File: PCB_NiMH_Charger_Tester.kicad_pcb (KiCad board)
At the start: 2 copper layers, 94.9 x 77.5 mm, 63 parts, among them J1 USB_C_Receptacle_PowerOnly_6P, J2 USB_C_Receptacle_USB2.0_16P, J3 UPDI v2 header, J4 SSD1306, J5 Serial Header, Q1 DTC114EL, Q2 DTA114EL, Q3 MTB060P06I3, Q4 MTA100N10KRI3, SW1 SW_Push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

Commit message: Revert resistor values
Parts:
- R10, R11: value 4.7k -> 1k
- R12, R15: value 47k -> 10k
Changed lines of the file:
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@@
 	(title_block
 		(title "NiMH Charger & Tester")
-		(date "2025-09-26")
+		(date "2025-10-15")
 		(rev "2")
 		(company "K.Takata")
@@
 			)
 		)
-		(property "Value" "4.7k"
+		(property "Value" "1k"
 			(at 1.27 2.37 0)
 			(layer "F.Fab")
@@
 			)
 		)
-		(property "Value" "47k"
+		(property "Value" "10k"
 			(at 1.27 2.37 0)
 			(layer "F.Fab")
@@
 			)
 		)
-		(property "Value" "47k"
+		(property "Value" "10k"
 			(at 1.27 2.37 0)
 			(layer "F.Fab")
@@
 			)
 		)
-		(property "Value" "4.7k"
+		(property "Value" "1k"
 			(at 1.27 2.37 0)
 			(layer "F.Fab")

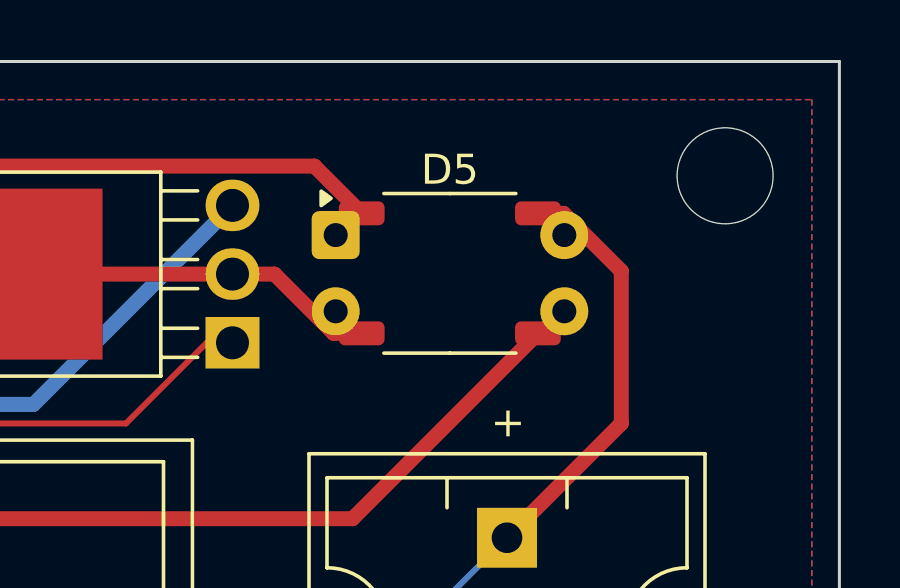
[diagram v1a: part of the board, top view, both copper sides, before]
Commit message: Fix D6 footprint
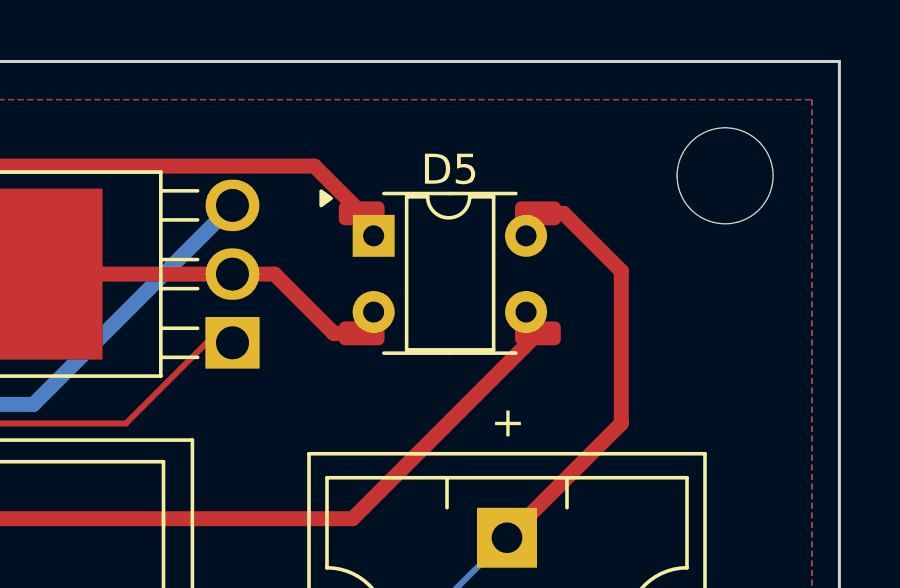
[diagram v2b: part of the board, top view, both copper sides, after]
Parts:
- D6: footprint Package_DIP:DIP-4_W7.62mm -> Diode_THT:Diode_Bridge_DIP-4_W5.08mm_P2.54mm
- moved D6 1.27 mm to (128.9, 29.9)
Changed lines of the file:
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@@
 		)
 	)
-	(footprint "Package_DIP:DIP-4_W7.62mm"
+	(footprint "Diode_THT:Diode_Bridge_DIP-4_W5.08mm_P2.54mm"
 		(layer "F.Cu")
-		(at 127.64 29.9162)
-		(descr "4-lead though-hole mounted DIP package, row spacing 7.62mm (300 mils)")
-		(tags "THT DIP DIL PDIP 2.54mm 7.62mm 300mil")
+		(at 128.905 29.9412)
+		(descr "4-lead dip package for diode bridges, row spacing 5.08mm, pin-spacing 2.54mm, see http://www.vishay.com/docs/88898/b2m.pdf")
+		(tags "DIL DIP PDIP 5.08mm 2.54")
 		(property "Reference" "D6"
-			(at 3.81 -2.33 0)
+			(at 2.5 -2.2 0)
 			(layer "F.SilkS")
 			(hide yes)
@@
 		)
 		(property "Value" "S1ZB20"
-			(at 3.81 4.87 0)
+			(at 2.3 4.6 0)
 			(layer "F.Fab")
 			(effects
@@
 		(property "Datasheet" "https://www.mouser.jp/datasheet/2/366/J534S1ZB-1203344.pdf"
 			(at 0 0 0)
+			(unlocked yes)
 			(layer "F.Fab")
 			(hide yes)
@@
 		(property "Description" "Diode Bridge, 200V Vrms, 1A If, DIP-4"
 			(at 0 0 0)
+			(unlocked yes)
 			(layer "F.Fab")
 			(hide yes)
@@
 		(sheetfile "PCB_NiMH_Charger_Tester.kicad_sch")
 		(attr through_hole dnp)
-		(fp_rect
-			(start -1.06 -1.52)
-			(end 8.67 4.07)
-			(stroke
-				(width 0.05)
-				(type solid)
-			)
-			(fill no)
-			(layer "F.CrtYd")
-		)
-		(fp_line
-			(start 0.635 -0.27)
-			(end 1.635 -1.27)
-			(stroke
-				(width 0.1)
-				(type solid)
-			)
-			(layer "F.Fab")
-		)
-		(fp_line
-			(start 0.635 3.81)
-			(end 0.635 -0.27)
-			(stroke
-				(width 0.1)
-				(type solid)
-			)
-			(layer "F.Fab")
-		)
-		(fp_line
-			(start 1.635 -1.27)
-			(end 6.985 -1.27)
-			(stroke
-				(width 0.1)
-				(type solid)
-			)
-			(layer "F.Fab")
-		)
-		(fp_line
-			(start 6.985 -1.27)
-			(end 6.985 3.81)
-			(stroke
-				(width 0.1)
-				(type solid)
-			)
-			(layer "F.Fab")
-		)
-		(fp_line
-			(start 6.985 3.81)
-			(end 0.635 3.81)
-			(stroke
-				(width 0.1)
+		(fp_line
+			(start 1.1 -1.3)
+			(end 1.1 3.8)
+			(stroke
+				(width 0.12)
+				(type solid)
+			)
+			(layer "F.SilkS")
+		)
+		(fp_line
+			(start 1.1 3.8)
+			(end 4 3.8)
+			(stroke
+				(width 0.12)
+				(type solid)
+			)
+			(layer "F.SilkS")
+		)
+		(fp_line
+			(start 1.8 -1.3)
+			(end 1.1 -1.3)
+			(stroke
+				(width 0.12)
+				(type solid)
+			)
+			(layer "F.SilkS")
+		)
+		(fp_line
+			(start 4 -1.3)
+			(end 3.2 -1.3)
+			(stroke
+				(width 0.12)
+				(type solid)
+			)
+			(layer "F.SilkS")
+		)
+		(fp_line
+			(start 4 3.8)
+			(end 4 -1.3)
+			(stroke
+				(width 0.12)
+				(type solid)
+			)
+			(layer "F.SilkS")
+		)
+		(fp_arc
+			(start 3.2 -1.3)
+			(mid 2.5 -0.6)
+			(end 1.8 -1.3)
+			(stroke
+				(width 0.12)
+				(type solid)
+			)
+			(layer "F.SilkS")
+		)
+		(fp_line
+			(start -0.95 -1.35)
+			(end -0.95 3.85)
+			(stroke
+				(width 0.05)
+				(type solid)
+			)
+			(layer "F.CrtYd")
+		)
+		(fp_line
+			(start -0.95 -1.35)
+			(end 6.03 -1.35)
+			(stroke
+				(width 0.05)
+				(type solid)
+			)
+			(layer "F.CrtYd")
+		)
+		(fp_line
+			(start 6.03 3.85)
+			(end -0.95 3.85)
+			(stroke
+				(width 0.05)
+				(type solid)
+			)
+			(layer "F.CrtYd")
+		)
+		(fp_line
+			(start 6.03 3.85)
+			(end 6.03 -1.35)
+			(stroke
+				(width 0.05)
+				(type solid)
+			)
+			(layer "F.CrtYd")
+		)
+		(fp_line
+			(start 0.5 -0.2)
+			(end 1.4 -1.1)
+			(stroke
+				(width 0.12)
+				(type solid)
+			)
+			(layer "F.Fab")
+		)
+		(fp_line
+			(start 0.5 3.6)
+			(end 0.5 -0.2)
+			(stroke
+				(width 0.12)
+				(type solid)
+			)
+			(layer "F.Fab")
+		)
+		(fp_line
+			(start 1.4 -1.1)
+			(end 4.6 -1.1)
+			(stroke
+				(width 0.12)
+				(type solid)
+			)
+			(layer "F.Fab")
+		)
+		(fp_line
+			(start 4.6 -1.1)
+			(end 4.6 3.6)
+			(stroke
+				(width 0.12)
+				(type solid)
+			)
+			(layer "F.Fab")
+		)
+		(fp_line
+			(start 4.6 3.6)
+			(end 0.5 3.6)
+			(stroke
+				(width 0.12)
 				(type solid)
 			)
@@
 		)
 		(fp_text user "${REFERENCE}"
-			(at 3.81 1.27 0)
-			(layer "F.Fab")
-			(effects
-				(font
-					(size 1 1)
-					(thickness 0.15)
-				)
-			)
-		)
-		(pad "1" thru_hole roundrect
+			(at 2.6 1.5 0)
+			(layer "F.Fab")
+			(effects
+				(font
+					(size 0.9 0.9)
+					(thickness 0.15)
+				)
+			)
+		)
+		(pad "1" thru_hole rect
 			(at 0 0)
-			(size 1.6 1.6)
-			(drill 0.8)
-			(layers "*.Cu" "*.Mask")
-			(remove_unused_layers no)
-			(roundrect_rratio 0.15625)
+			(size 1.4 1.4)
+			(drill 0.7)
+			(layers "*.Cu" "*.Mask")
+			(remove_unused_layers no)
 			(net 19 "Net-(D5-+)")
 			(pinfunction "+")
@@
 		(pad "2" thru_hole circle
 			(at 0 2.54)
-			(size 1.6 1.6)
-			(drill 0.8)
+			(size 1.4 1.4)
+			(drill 0.7)
 			(layers "*.Cu" "*.Mask")
 			(remove_unused_layers no)
@@
 		)
 		(pad "3" thru_hole circle
-			(at 7.62 2.54)
-			(size 1.6 1.6)
-			(drill 0.8)
+			(at 5.08 2.54)
+			(size 1.4 1.4)
+			(drill 0.7)
 			(layers "*.Cu" "*.Mask")
 			(remove_unused_layers no)
@@
 		)
 		(pad "4" thru_hole circle
-			(at 7.62 0)
-			(size 1.6 1.6)
-			(drill 0.8)
+			(at 5.08 0)
+			(size 1.4 1.4)
+			(drill 0.7)
 			(layers "*.Cu" "*.Mask")
 			(remove_unused_layers no)
@@
 		)
 		(embedded_fonts no)
-		(model "${KICAD9_3DMODEL_DIR}/Package_DIP.3dshapes/DIP-4_W7.62mm.step"
+		(model "${KICAD9_3DMODEL_DIR}/Diode_THT.3dshapes/Diode_Bridge_DIP-4_W5.08mm_P2.54mm.step"
 			(offset
 				(xyz 0 0 0)
